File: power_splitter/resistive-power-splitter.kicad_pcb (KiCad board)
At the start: 4 copper layers, 120 x 99 mm, 36 parts, among them J1 Conn_01x02, J10 Conn_01x02, J11 Conn_01x02, J12 Conn_01x02, J2 Conn_01x02, J3 Conn_01x02, J4 Conn_01x02, J5 Conn_01x02, J6 Conn_01x02, J7 Conn_01x02, J8 Conn_01x02, J9 Conn_01x02

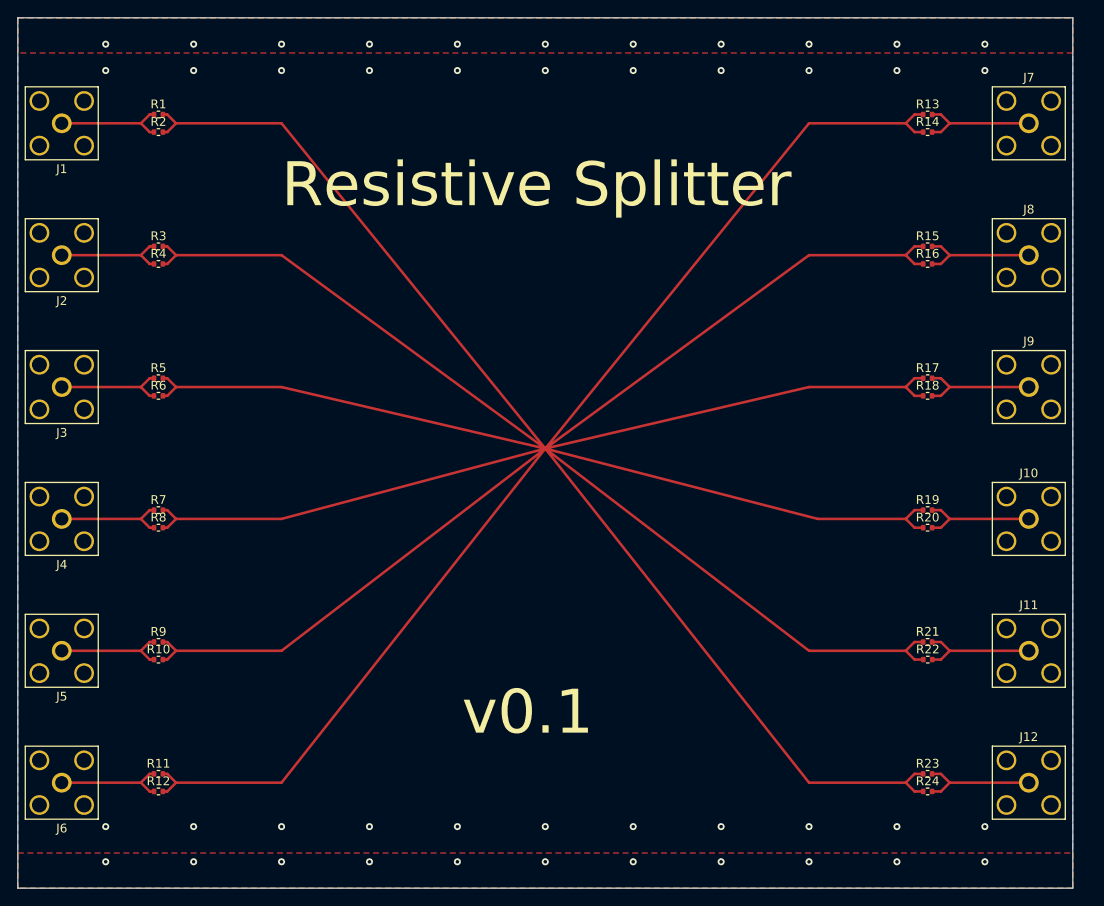
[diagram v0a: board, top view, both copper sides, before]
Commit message: power splitter: PCB v0.2 & pcbnew scripts
- new power splitter PCB: dodecagon outline
- scripts to create PCB edge cuts & component placement
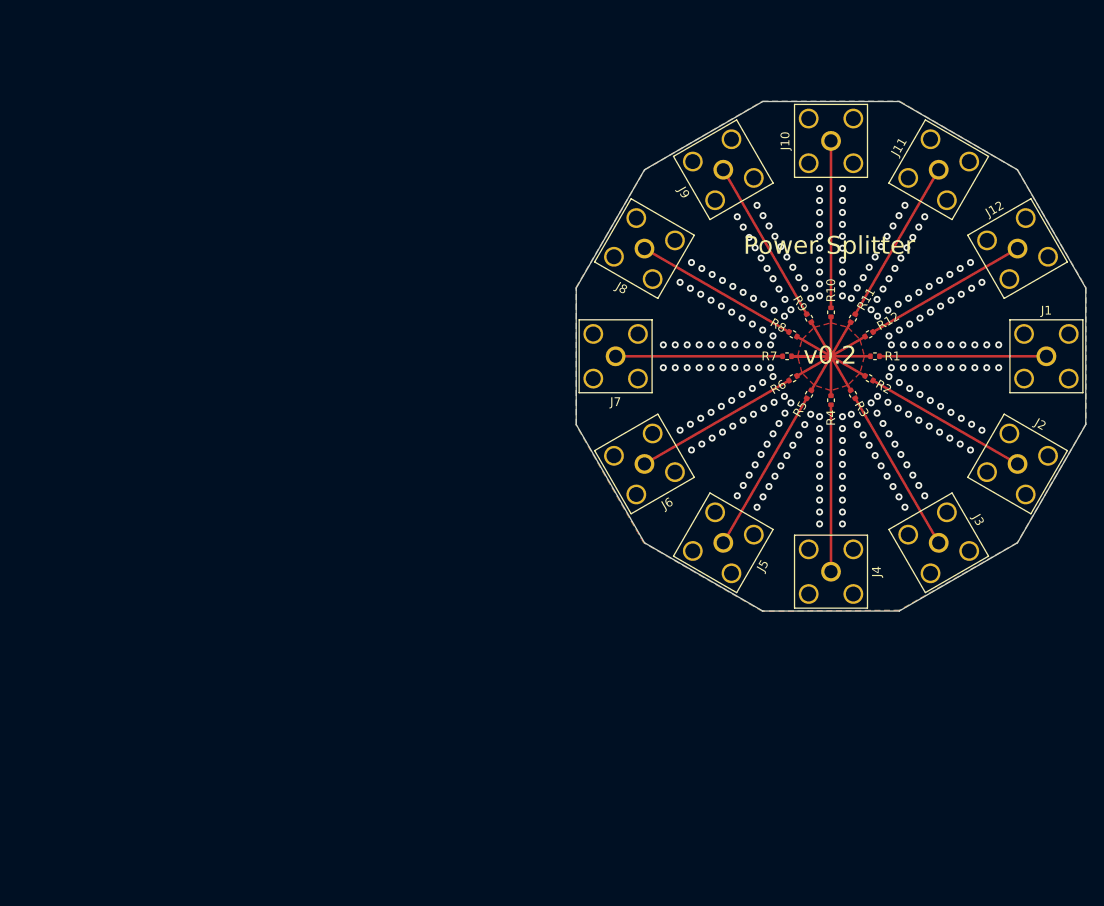
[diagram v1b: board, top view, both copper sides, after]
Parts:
- removed R13, R14, R15, R16, R17, R18, R19, R20, R21, R22, R23, R24: 82, Resistor_SMD:R_0402_1005Metric
- R1, R10, R11, R12, R2, R3, R4, R5, R6, R7, R8, R9: value 82 -> 41.2
- moved J1 115.1 mm to (177.0, 89.5), turned to 270 degrees
- moved J2 111.3 mm to (173.7, 101.8), turned to 240 degrees
- moved J3 101.3 mm to (164.8, 110.7), turned to 210 degrees
- moved R12 96.1 mm to (156.8, 87.0), turned to 30 degrees
- moved R11 94.5 mm to (155.0, 85.2), turned to 60 degrees
- moved J4 87.7 mm to (152.5, 114.0), turned to 180 degrees
- moved R10 86.1 mm to (152.5, 84.5), turned to 90 degrees
- moved R1 86.0 mm to (157.5, 89.5), turned to 180 degrees
- moved R2 85.5 mm to (156.8, 92.0), turned to 150 degrees
- moved R9 82.7 mm to (150.0, 85.2), turned to 120 degrees
- moved R3 80.8 mm to (155.0, 93.8), turned to 120 degrees
- moved R4 78.1 mm to (152.5, 94.5), turned to 90 degrees
- moved J5 76.2 mm to (140.2, 110.7), turned to 150 degrees
- moved J6 75.5 mm to (131.3, 101.8), turned to 120 degrees
- moved R8 75.4 mm to (148.2, 87.0), turned to 150 degrees
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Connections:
- R10 pad 1: Net-(J5-Pad1) -> Net-(R1-Pad2)
- R10 pad 2: Net-(R1-Pad2) -> Net-(J10-Pad1)
- R11 pad 1: Net-(J6-Pad1) -> Net-(R1-Pad2)
- R11 pad 2: Net-(R1-Pad2) -> Net-(J11-Pad1)
- R12 pad 1: Net-(J6-Pad1) -> Net-(R1-Pad2)
- R12 pad 2: Net-(R1-Pad2) -> Net-(J12-Pad1)
- R2 pad 1: Net-(J1-Pad1) -> Net-(J2-Pad1)
- R3 pad 1: Net-(J2-Pad1) -> Net-(J3-Pad1)
- R4 pad 1: Net-(J2-Pad1) -> Net-(J4-Pad1)
- R5 pad 1: Net-(J3-Pad1) -> Net-(J5-Pad1)
- R6 pad 1: Net-(J3-Pad1) -> Net-(J6-Pad1)
- R7 pad 1: Net-(J4-Pad1) -> Net-(R1-Pad2)
- R7 pad 2: Net-(R1-Pad2) -> Net-(J7-Pad1)
- R8 pad 1: Net-(J4-Pad1) -> Net-(R1-Pad2)
- R8 pad 2: Net-(R1-Pad2) -> Net-(J8-Pad1)
- R9 pad 1: Net-(J5-Pad1) -> Net-(R1-Pad2)
- R9 pad 2: Net-(R1-Pad2) -> Net-(J9-Pad1)
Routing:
- net Net-(R1-Pad2): track 655.4 -> 58.4 mm
- net Net-(J1-Pad1): track 12.8 -> 19.0 mm
- net Net-(J4-Pad1): track 12.8 -> 19.0 mm
- net Net-(J5-Pad1): track 12.8 -> 19.0 mm
- net Net-(J3-Pad1): track 12.8 -> 19.0 mm
- net Net-(J6-Pad1): track 12.8 -> 19.0 mm
- net Net-(J2-Pad1): track 12.8 -> 19.0 mm
- net Net-(J11-Pad1): track 13.8 -> 19.0 mm
- net Net-(J7-Pad1): track 13.8 -> 19.0 mm
- net Net-(J10-Pad1): track 13.8 -> 19.0 mm
- net Net-(J9-Pad1): track 13.8 -> 19.0 mm
- net Net-(J8-Pad1): track 13.8 -> 19.0 mm
- net Net-(J12-Pad1): track 13.8 -> 19.0 mm
- net GND: vias 44 -> 240
- added copper zone on F.Cu, net Net-(R1-Pad2)
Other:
- board size 120 x 99 mm -> 58 x 58 mm
- board text added: "Power Splitter"
- board text added: "v0.2"
- board text removed: "Resistive Splitter"
- board text removed: "v0.1"
